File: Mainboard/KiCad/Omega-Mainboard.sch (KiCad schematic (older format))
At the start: 13 parts, among them J1 5V, J10 POWER

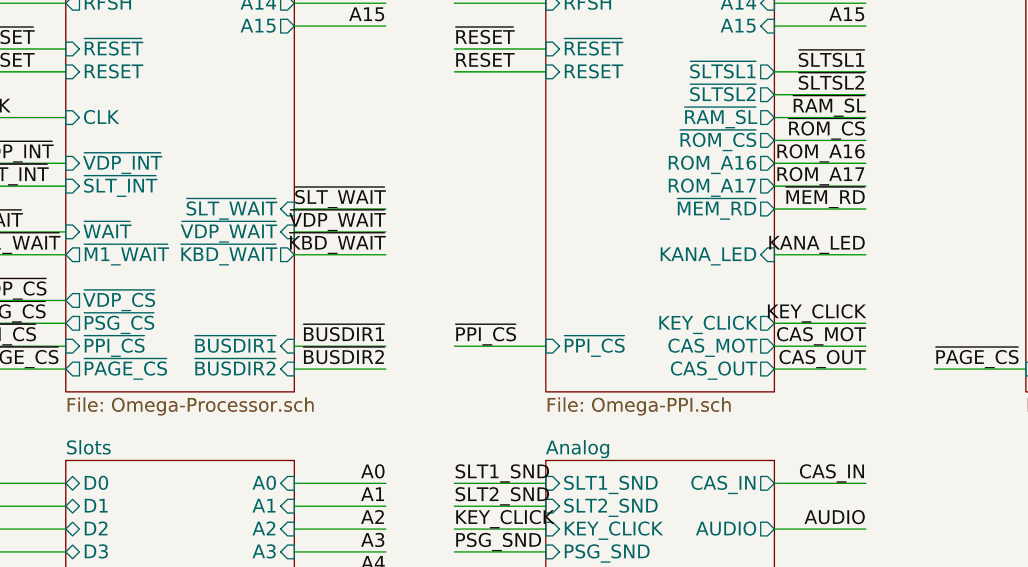
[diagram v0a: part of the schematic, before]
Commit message: Mainboard: Fix some of the issues described in #1
Signed-off-by: Sergey Kiselev <skiselev@gmail.com>
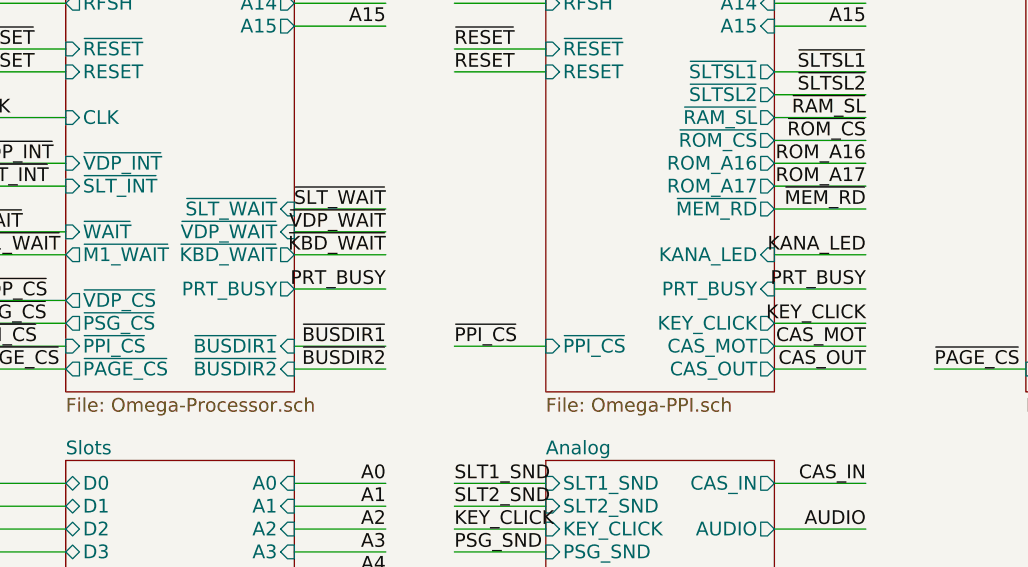
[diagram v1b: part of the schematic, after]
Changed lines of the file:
@@
 F43 "ROM_A17" O R 4200 3200 60
 F44 "~MEM_RD" O R 4200 3300 60
+F45 "PRT_BUSY" I R 4200 3650 60
 $EndSheet
 Wire Wire Line
@@
 F46 "~M1_WAIT" O L 1100 3500 60
 F47 "~KBD_WAIT" O R 2100 3500 60
+F48 "PRT_BUSY" O R 2100 3650 60
 $EndSheet
 Wire Wire Line
@@
 Wire Wire Line
 	6100 6600 6100 6700
+Wire Wire Line
+	2100 3650 2500 3650
+Text Label 2500 3650 2    60   ~ 0
+PRT_BUSY
+Wire Wire Line
+	4200 3650 4600 3650
+Text Label 4600 3650 2    60   ~ 0
+PRT_BUSY
 $EndSCHEMATC

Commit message: Add files for version 1.3eu from Jordi Solis
Signed-off-by: Sergey Kiselev <skiselev@gmail.com>
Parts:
- HOLE1, HOLE10, HOLE11, HOLE2, HOLE3, HOLE4, HOLE5, HOLE6, HOLE7, HOLE8, HOLE9: symbol my_components:HOLE -> Omega-Mainboard-rescue:HOLE-my_components
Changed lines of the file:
@@
 EESchema Schematic File Version 4
 LIBS:Omega-Mainboard-cache
-EELAYER 29 0
+EELAYER 30 0
 EELAYER END
 $Descr A4 11693 8268
@@
 AUDIO
 $Comp
-L my_components:HOLE HOLE1
+L Omega-Mainboard-rescue:HOLE-my_components HOLE1
 U 1 1 5C161AFB
 P 6450 4600
@@
 $EndComp
 $Comp
-L my_components:HOLE HOLE2
+L Omega-Mainboard-rescue:HOLE-my_components HOLE2
 U 1 1 5C1A08F5
 P 6450 4800
@@
 $EndComp
 $Comp
-L my_components:HOLE HOLE3
+L Omega-Mainboard-rescue:HOLE-my_components HOLE3
 U 1 1 5C1A0DFB
 P 6450 5000
@@
 $EndComp
 $Comp
-L my_components:HOLE HOLE4
+L Omega-Mainboard-rescue:HOLE-my_components HOLE4
 U 1 1 5C1A184C
 P 6450 5200
@@
 $EndComp
 $Comp
-L my_components:HOLE HOLE5
+L Omega-Mainboard-rescue:HOLE-my_components HOLE5
 U 1 1 5C1A1852
 P 6450 5400
@@
 $EndComp
 $Comp
-L my_components:HOLE HOLE6
+L Omega-Mainboard-rescue:HOLE-my_components HOLE6
 U 1 1 5C1A1858
 P 6450 5600
@@
 Connection ~ 6100 5600
 $Comp
-L my_components:HOLE HOLE7
+L Omega-Mainboard-rescue:HOLE-my_components HOLE7
 U 1 1 5C1A42ED
 P 6450 5800
@@
 $EndComp
 $Comp
-L my_components:HOLE HOLE8
+L Omega-Mainboard-rescue:HOLE-my_components HOLE8
 U 1 1 5C1A42F3
 P 6450 6000
@@
 $EndComp
 $Comp
-L my_components:HOLE HOLE9
+L Omega-Mainboard-rescue:HOLE-my_components HOLE9
 U 1 1 5C1A42F9
 P 6450 6200
@@
 $EndComp
 $Comp
-L my_components:HOLE HOLE10
+L Omega-Mainboard-rescue:HOLE-my_components HOLE10
 U 1 1 5C1A42FF
 P 6450 6400
@@
 Connection ~ 6100 6400
 $Comp
-L my_components:HOLE HOLE11
+L Omega-Mainboard-rescue:HOLE-my_components HOLE11
 U 1 1 5C131D5E
 P 6450 6600

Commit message: Version 1.4: Add cut-out for the right angle slot connector. Add optional jumpers to limit memory mapper address range
Signed-off-by: Sergey Kiselev <skiselev@gmail.com>
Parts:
- HOLE1, HOLE10, HOLE11, HOLE2, HOLE3, HOLE4, HOLE5, HOLE6, HOLE7, HOLE8, HOLE9: symbol Omega-Mainboard-rescue:HOLE-my_components -> my_components:HOLE
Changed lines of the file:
@@
 EESchema Schematic File Version 4
-LIBS:Omega-Mainboard-cache
 EELAYER 30 0
 EELAYER END
@@
 AUDIO
 $Comp
-L Omega-Mainboard-rescue:HOLE-my_components HOLE1
+L my_components:HOLE HOLE1
 U 1 1 5C161AFB
 P 6450 4600
@@
 $EndComp
 $Comp
-L Omega-Mainboard-rescue:HOLE-my_components HOLE2
+L my_components:HOLE HOLE2
 U 1 1 5C1A08F5
 P 6450 4800
@@
 $EndComp
 $Comp
-L Omega-Mainboard-rescue:HOLE-my_components HOLE3
+L my_components:HOLE HOLE3
 U 1 1 5C1A0DFB
 P 6450 5000
@@
 $EndComp
 $Comp
-L Omega-Mainboard-rescue:HOLE-my_components HOLE4
+L my_components:HOLE HOLE4
 U 1 1 5C1A184C
 P 6450 5200
@@
 $EndComp
 $Comp
-L Omega-Mainboard-rescue:HOLE-my_components HOLE5
+L my_components:HOLE HOLE5
 U 1 1 5C1A1852
 P 6450 5400
@@
 $EndComp
 $Comp
-L Omega-Mainboard-rescue:HOLE-my_components HOLE6
+L my_components:HOLE HOLE6
 U 1 1 5C1A1858
 P 6450 5600
@@
 Connection ~ 6100 5600
 $Comp
-L Omega-Mainboard-rescue:HOLE-my_components HOLE7
+L my_components:HOLE HOLE7
 U 1 1 5C1A42ED
 P 6450 5800
@@
 $EndComp
 $Comp
-L Omega-Mainboard-rescue:HOLE-my_components HOLE8
+L my_components:HOLE HOLE8
 U 1 1 5C1A42F3
 P 6450 6000
@@
 $EndComp
 $Comp
-L Omega-Mainboard-rescue:HOLE-my_components HOLE9
+L my_components:HOLE HOLE9
 U 1 1 5C1A42F9
 P 6450 6200
@@
 $EndComp
 $Comp
-L Omega-Mainboard-rescue:HOLE-my_components HOLE10
+L my_components:HOLE HOLE10
 U 1 1 5C1A42FF
 P 6450 6400
@@
 Connection ~ 6100 6400
 $Comp
-L Omega-Mainboard-rescue:HOLE-my_components HOLE11
+L my_components:HOLE HOLE11
 U 1 1 5C131D5E
 P 6450 6600
